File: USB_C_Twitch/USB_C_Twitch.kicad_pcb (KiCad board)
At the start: 4 copper layers, 60 x 60 mm, 69 parts, among them J1 Conn_01x06_Pin, J2 Conn_01x06_Pin, Q1 Q_PNP_BEC, Q2 Q_PNP_BEC, Q3 Q_PNP_BEC, Q4 Q_PMOS_GSD, Q5 Q_PMOS_GSD, Q6 Q_PNP_BEC, Q7 Q_PNP_BEC, Q8 Q_PMOS_GSD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

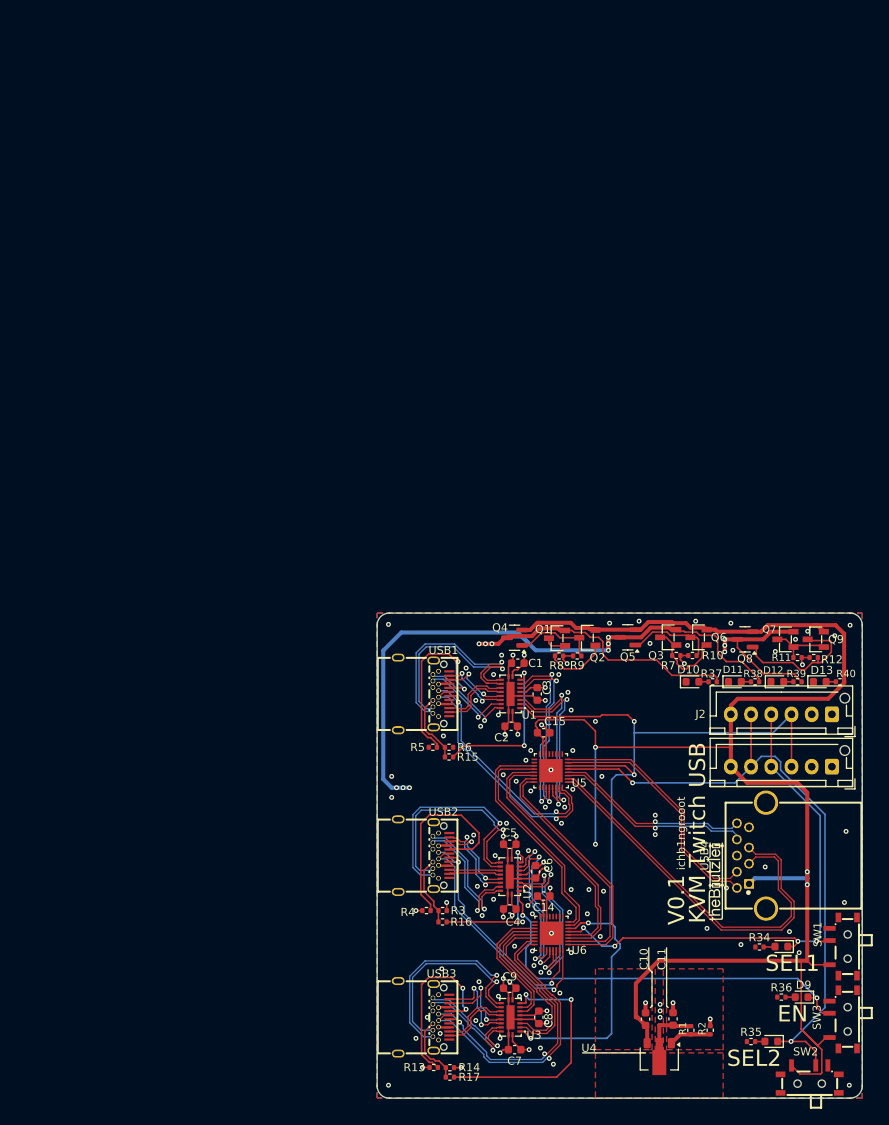
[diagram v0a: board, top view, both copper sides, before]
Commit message: add nev versions. (usb c and displayport working)
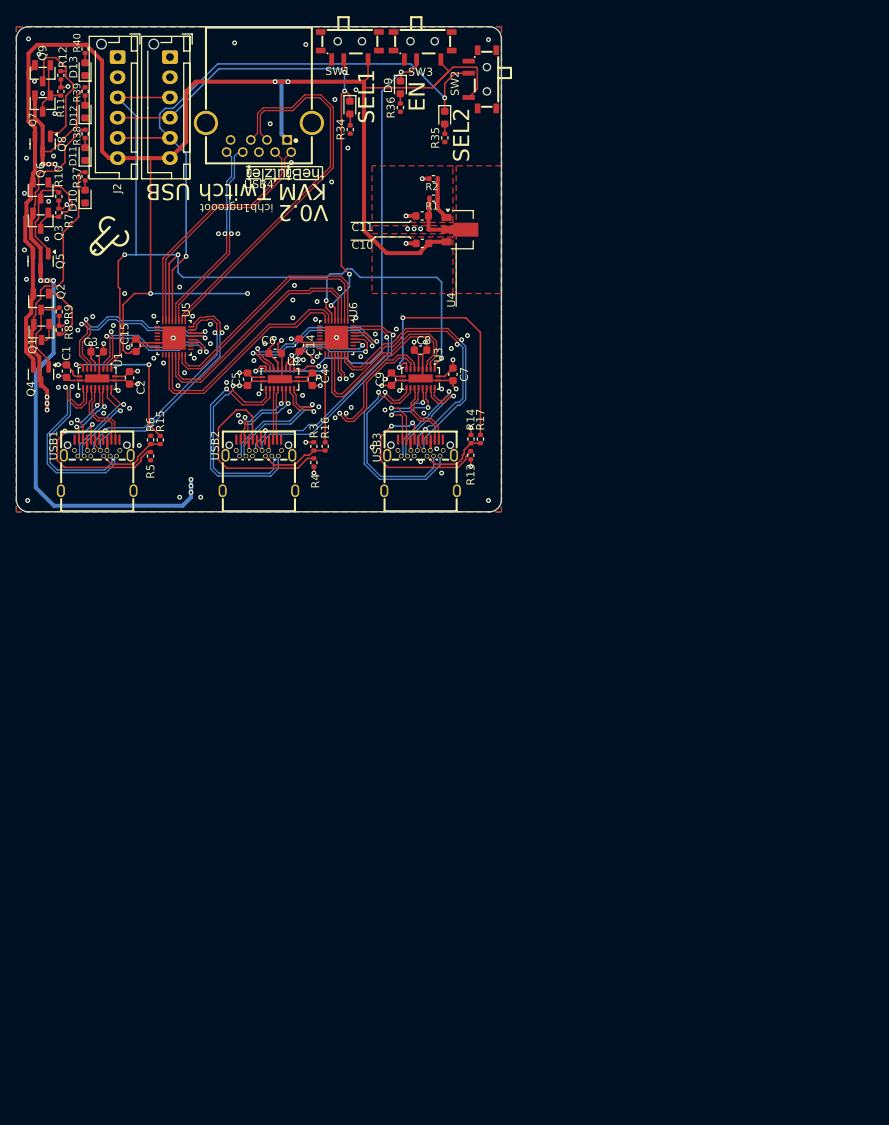
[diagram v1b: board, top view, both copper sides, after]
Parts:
- moved SW3 131.2 mm to (176.6, 23.8), turned to 180 degrees
- moved SW2 130.1 mm to (184.0, 28.0), turned to 90 degrees
- moved SW1 127.0 mm to (167.6, 23.8), turned to 180 degrees
- moved D9 123.0 mm to (173.9, 29.0), turned to -90 degrees
- moved R40 121.8 mm to (134.9, 24.2), turned to -90 degrees
- moved D8 121.2 mm to (179.4, 32.7), turned to -90 degrees
- moved J2 120.1 mm to (138.9, 25.2), turned to -90 degrees
- moved J1 120.0 mm to (145.4, 25.2), turned to -90 degrees
- moved R36 119.7 mm to (173.9, 31.5), turned to 90 degrees
- moved Q9 118.5 mm to (129.6, 27.2), turned to 90 degrees
- moved D13 118.3 mm to (134.9, 26.7), turned to 90 degrees
- moved R35 118.0 mm to (179.4, 35.2), turned to 90 degrees
- moved R12 117.7 mm to (131.9, 27.5), turned to -90 degrees
- moved D7 116.7 mm to (167.6, 31.5), turned to -90 degrees
- moved R11 114.9 mm to (131.9, 29.5), turned to 90 degrees
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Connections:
- U1 pad 2: /A_SSRX+ -> /A_SSTX+
- U1 pad 3: /A_SSRX- -> /A_SSTX-
- U1 pad 6: /A_SSTX+ -> /A_SSRX+
- U1 pad 7: /A_SSTX- -> /A_SSRX-
- U2 pad 2: /B_SSRX+ -> /B_SSTX+
- U2 pad 3: /B_SSRX- -> /B_SSTX-
- U2 pad 6: /B_SSTX+ -> /B_SSRX+
- U2 pad 7: /B_SSTX- -> /B_SSRX-
- U3 pad 2: /C_SSRX+ -> /C_SSTX+
- U3 pad 3: /C_SSRX- -> /C_SSTX-
- U3 pad 6: /C_SSTX+ -> /C_SSRX+
- U3 pad 7: /C_SSTX- -> /C_SSRX-
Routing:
- net /C_SSTX-: track 16.2 -> 24.5 mm
- net /C_SSTX+: track 16.2 -> 24.5 mm
- net /B_SSTX-: track 19.9 -> 13.2 mm
- net /B_SSTX+: track 20.0 -> 14.5 mm
- net /A_SSRX+: track 22.2 -> 25.8 mm
- net /B_SSRX-: track 20.3 -> 23.4 mm
- net /A_SSRX-: track 22.8 -> 25.8 mm
- net /A_SSTX-: track 22.8 -> 20.4 mm
- net /C_SSRX+: track 21.3 -> 23.2 mm, vias 0 -> 2
- net /C_SSRX-: track 21.3 -> 23.2 mm, vias 0 -> 2
- net /B_SSRX+: track 22.2 -> 24.0 mm
- net /A_SSTX+: track 22.9 -> 21.5 mm
- net +5V: track 235.2 -> 236.3 mm
- net +3V3: track 199.0 -> 199.5 mm
- net GND: track 72.6 -> 72.5 mm, vias 103 -> 105
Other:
- board text added: "V0.2"
- board text removed: "V0.1"
